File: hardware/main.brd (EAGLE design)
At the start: 64.8 x 34 mm, 10 parts, among them U1 TXB0101_DBV_6

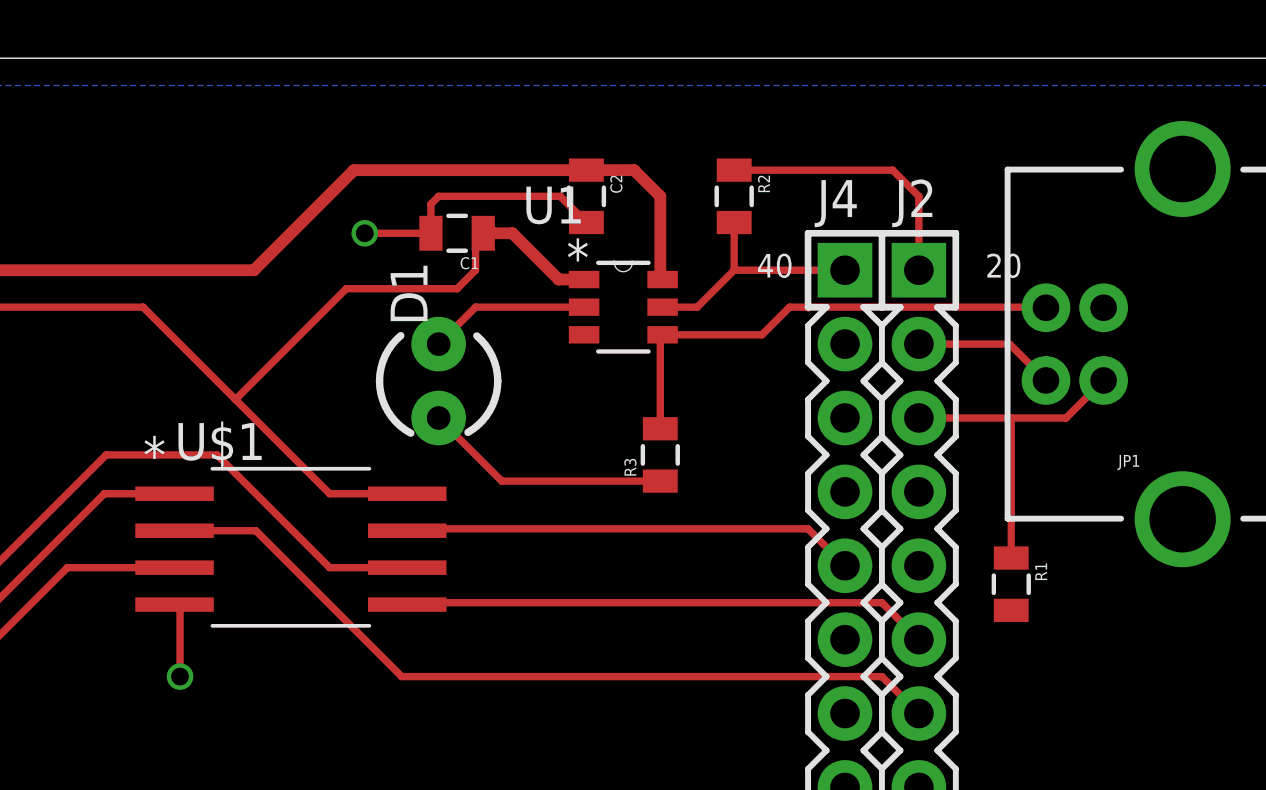
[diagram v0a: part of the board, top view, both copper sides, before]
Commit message: Updated small labels. Cleaned up silkscreen layer.
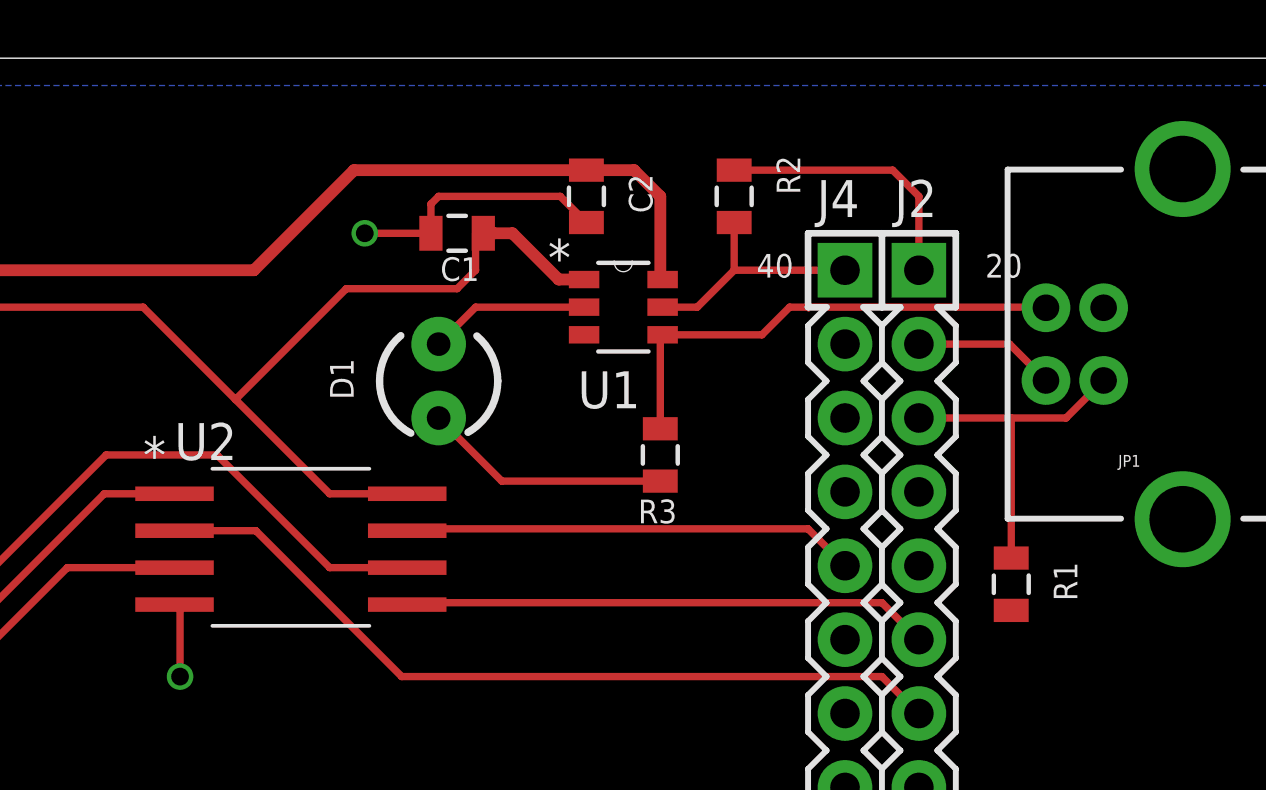
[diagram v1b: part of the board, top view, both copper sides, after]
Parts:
- renumbered U$1 to U2
